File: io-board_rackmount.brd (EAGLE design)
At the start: 124 x 90.3 mm, 12 parts, among them X1 22-23-2041, X3 22-23-2101

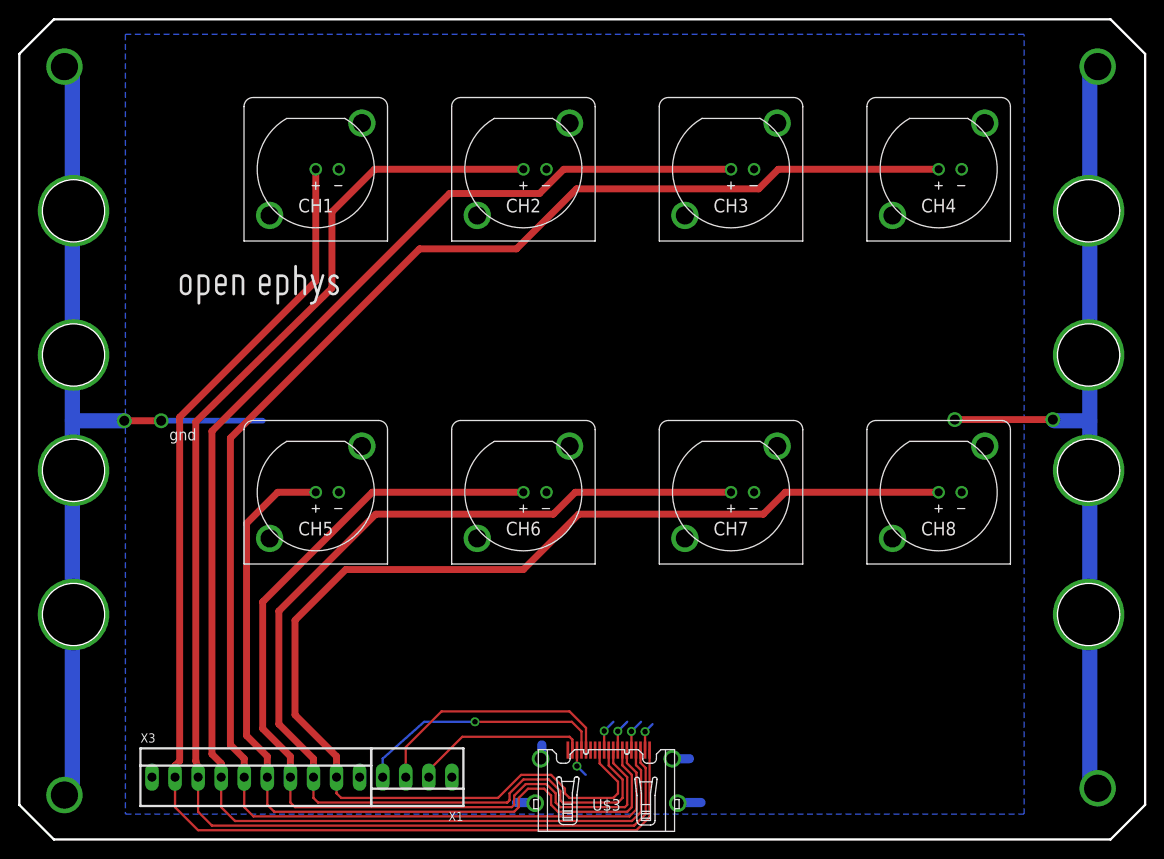
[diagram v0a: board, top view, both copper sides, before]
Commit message: Restore large holes and add 3 mm holes for mounting a case
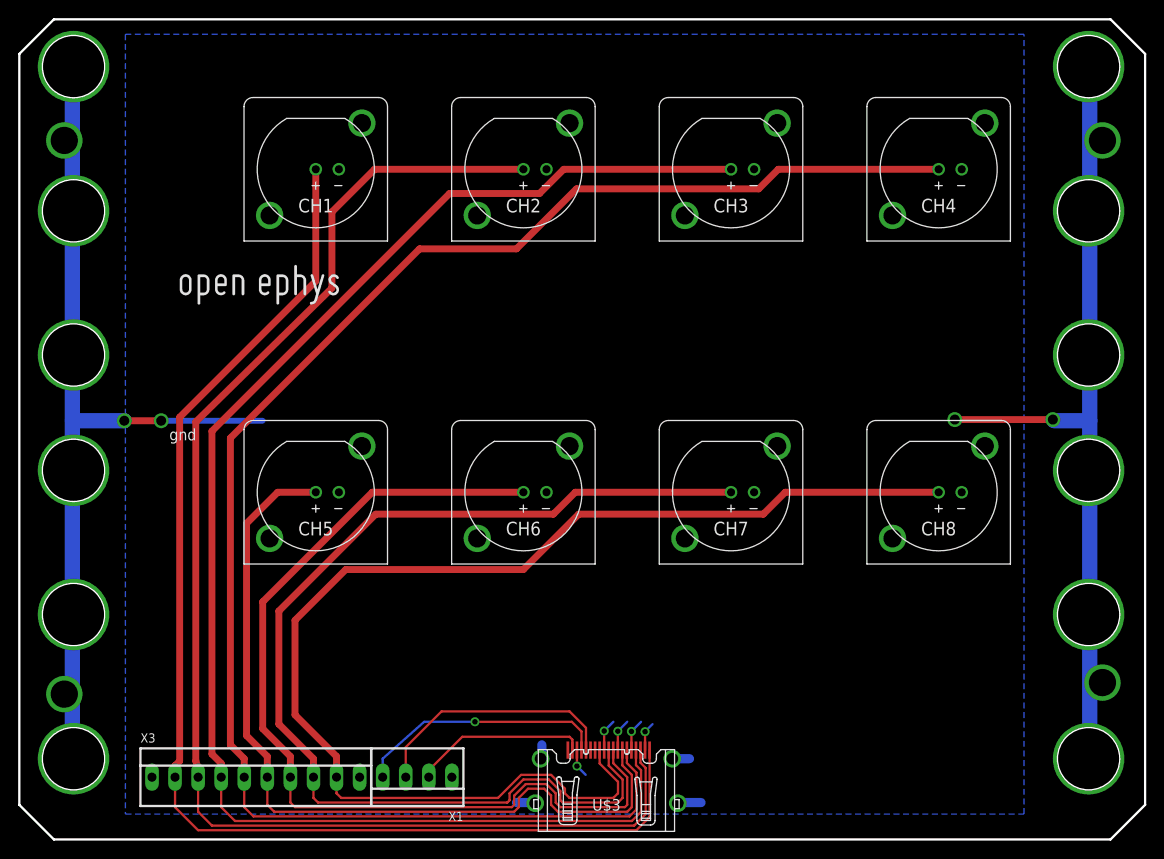
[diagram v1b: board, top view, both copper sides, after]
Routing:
- net S$13: track 79.9 -> 73.9 mm
- net S$14: track 78.2 -> 76.2 mm
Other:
- board text added: "May 2013"
- board text added: "version 1.3"
- board text removed: "July 2013"
- board text removed: "version 1.4"
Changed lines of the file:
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@@
 <setting verticaltext="up"/>
 </settings>
-<grid distance="0.01" unitdist="inch" unit="inch" style="lines" multiple="1" display="yes" altdistance="0.025" altunitdist="inch" altunit="inch"/>
+<grid distance="0.05" unitdist="inch" unit="inch" style="lines" multiple="1" display="yes" altdistance="0.025" altunitdist="inch" altunit="inch"/>
 <layers>
 <layer number="1" name="Top" color="4" fill="1" visible="yes" active="yes"/>
@@
 <layer number="43" name="vRestrict" color="2" fill="10" visible="no" active="yes"/>
 <layer number="44" name="Drills" color="7" fill="1" visible="no" active="yes"/>
-<layer number="45" name="Holes" color="7" fill="1" visible="no" active="yes"/>
+<layer number="45" name="Holes" color="7" fill="1" visible="yes" active="yes"/>
 <layer number="46" name="Milling" color="3" fill="1" visible="no" active="yes"/>
 <layer number="47" name="Measures" color="7" fill="1" visible="no" active="yes"/>
@@
 <plain>
 <text x="17.907" y="56.642" size="1.778" layer="51" font="vector">I/O Board</text>
-<text x="17.907" y="54.102" size="1.27" layer="51" font="vector">version 1.4</text>
-<text x="18.034" y="51.181" size="1.27" layer="51" font="vector">July 2013</text>
+<text x="17.907" y="54.102" size="1.27" layer="51" font="vector">version 1.3</text>
+<text x="18.034" y="51.181" size="1.27" layer="51" font="vector">May 2013</text>
+<hole x="6.096" y="85.598" drill="6.858"/>
 <hole x="6.096" y="69.723" drill="6.858"/>
 <hole x="6.096" y="53.848" drill="6.858"/>
 <hole x="6.096" y="41.148" drill="6.858"/>
 <hole x="6.096" y="25.273" drill="6.858"/>
+<hole x="6.096" y="9.398" drill="6.858"/>
 <wire x1="120.269" y1="0.508" x2="3.937" y2="0.508" width="0.254" layer="20"/>
 <wire x1="3.937" y1="0.508" x2="0.127" y2="4.318" width="0.254" layer="20"/>
@@
 <text x="38.227" y="9.906" size="1.27" layer="51" font="vector" ratio="12" rot="R90">gnd</text>
 <text x="16.764" y="11.049" size="1.3716" layer="51" font="vector" ratio="18">8 7 6 5 4 3 2 1</text>
+<hole x="117.856" y="85.598" drill="6.858"/>
 <hole x="117.856" y="69.723" drill="6.858"/>
 <hole x="117.856" y="53.848" drill="6.858"/>
 <hole x="117.856" y="41.148" drill="6.858"/>
 <hole x="117.856" y="25.273" drill="6.858"/>
+<hole x="117.856" y="9.398" drill="6.858"/>
 </plain>
 <attributes>
@@
 </signal>
 <signal name="S$1">
-<via x="5.096" y="85.598" extent="1-16" drill="3"/>
+<via x="6.096" y="85.598" extent="1-16" drill="6.858"/>
 </signal>
 <signal name="S$2">
@@
 </signal>
 <signal name="S$6">
-<via x="5.096" y="5.398" extent="1-16" drill="3"/>
+<via x="6.096" y="9.398" extent="1-16" drill="6.858"/>
 </signal>
 <signal name="S$13">
-<wire x1="5.969" y1="84.836" x2="5.969" y2="4.922" width="1.6764" layer="16"/>
+<wire x1="5.969" y1="84.836" x2="5.969" y2="10.922" width="1.6764" layer="16"/>
 </signal>
 <signal name="VCC">
@@
 <wire x1="114.046" y1="46.609" x2="117.983" y2="46.609" width="1.6764" layer="16"/>
 </signal>
-<signal name="3">
-<via x="118.856" y="85.598" extent="1-16" drill="3"/>
+<signal name="S$7">
+<via x="117.856" y="85.598" extent="1-16" drill="6.858"/>
 </signal>
 <signal name="S$8">
@@
 </signal>
 <signal name="S$12">
-<via x="118.856" y="6.144" extent="1-16" drill="3"/>
+<via x="117.856" y="9.398" extent="1-16" drill="6.858"/>
 </signal>
 <signal name="S$14">
-<wire x1="117.983" y1="85.09" x2="117.983" y2="6.89" width="1.6764" layer="16"/>
+<wire x1="117.983" y1="85.09" x2="117.983" y2="8.89" width="1.6764" layer="16"/>
+</signal>
+<signal name="N$1">
+<via x="5.08" y="77.47" extent="1-16" drill="3" shape="square"/>
+</signal>
+<signal name="N$6">
+<via x="5.08" y="16.51" extent="1-16" drill="3" shape="square"/>
+</signal>
+<signal name="N$9">
+<via x="119.38" y="17.78" extent="1-16" drill="3" shape="square"/>
+</signal>
+<signal name="N$10">
+<via x="119.38" y="77.47" extent="1-16" drill="3" shape="square"/>
 </signal>
 </signals>
